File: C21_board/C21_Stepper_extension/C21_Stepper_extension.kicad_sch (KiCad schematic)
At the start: 22 parts, among them J1 Conn_01x04_Male, J10 Conn_01x02_Male, J11 Conn_01x02_Male, J12 Conn_01x04_Male, J2 Conn_01x02_Male, J3 Conn_01x02_Male, J4 Conn_01x02_Male, J5 Jack-DC, J6 Screw_Terminal_01x02, J7 Conn_01x04_Male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

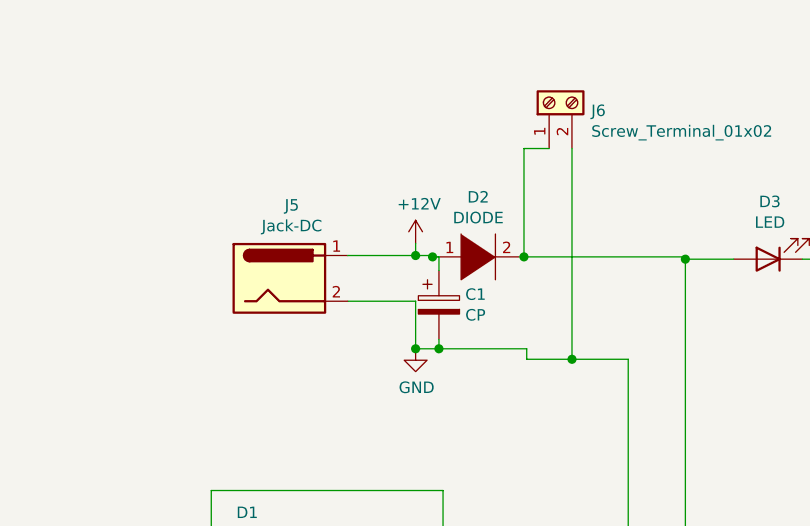
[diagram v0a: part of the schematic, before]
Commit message: add robot arm
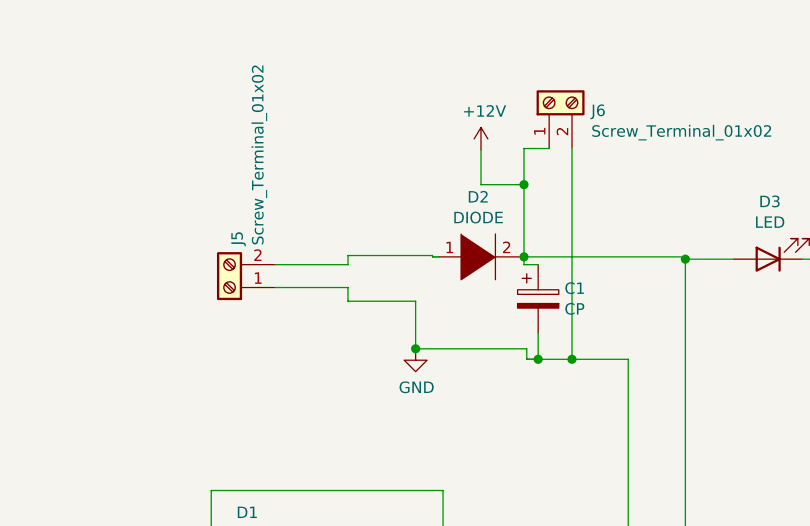
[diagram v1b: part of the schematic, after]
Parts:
- removed J5: Jack-DC, Connector_BarrelJack:BarrelJack_Wuerth_6941xx301002, symbol Connector:Jack-DC
- added J5: Screw_Terminal_01x02, TerminalBlock:TerminalBlock_Altech_AK300-2_P5.00mm, symbol Connector:Screw_Terminal_01x02
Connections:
- net +12V: now also A1.8 (VMOT), A2.8 (VMOT), C2.1, C3.1, D2.2 (A), D3.2 (A), J6.1 (Pin_1); no longer D2.1 (K)
- net GND: now also J5.1 (Pin_1)
- new net: D2.1 (K), J5.2 (Pin_2)
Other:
- moved on the sheet: C1
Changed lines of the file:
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@@
   (junction (at 73.8124 108.0008) (diameter 1.016) (color 0 0 0 0))
   (junction (at 73.8124 114.6556) (diameter 1.016) (color 0 0 0 0))
-  (junction (at 87.9856 44.704) (diameter 1.016) (color 0 0 0 0))
   (junction (at 87.9856 55.0672) (diameter 1.016) (color 0 0 0 0))
-  (junction (at 89.8652 44.8564) (diameter 1.016) (color 0 0 0 0))
-  (junction (at 90.5764 55.0672) (diameter 1.016) (color 0 0 0 0))
   (junction (at 91.0336 88.1888) (diameter 1.016) (color 0 0 0 0))
   (junction (at 91.0336 90.7288) (diameter 1.016) (color 0 0 0 0))
+  (junction (at 100.0252 36.83) (diameter 1.016) (color 0 0 0 0))
   (junction (at 100.0252 44.8564) (diameter 1.016) (color 0 0 0 0))
   (junction (at 101.1936 118.6688) (diameter 1.016) (color 0 0 0 0))
+  (junction (at 101.6 56.2356) (diameter 1.016) (color 0 0 0 0))
   (junction (at 103.7336 118.6688) (diameter 1.016) (color 0 0 0 0))
   (junction (at 105.3592 56.2356) (diameter 1.016) (color 0 0 0 0))
@@
     (stroke (width 0) (type solid) (color 0 0 0 0))
   )
+  (wire (pts (xy 72.39 45.72) (xy 80.4672 45.72))
+    (stroke (width 0) (type solid) (color 0 0 0 0))
+  )
   (wire (pts (xy 72.898 79.6544) (xy 76.6572 79.6544))
     (stroke (width 0) (type solid) (color 0 0 0 0))
@@
     (stroke (width 0) (type solid) (color 0 0 0 0))
   )
-  (wire (pts (xy 80.4672 44.704) (xy 87.9856 44.704))
+  (wire (pts (xy 80.4672 44.704) (xy 89.8652 44.704))
+    (stroke (width 0) (type solid) (color 0 0 0 0))
+  )
+  (wire (pts (xy 80.4672 45.72) (xy 80.4672 44.704))
+    (stroke (width 0) (type solid) (color 0 0 0 0))
+  )
+  (wire (pts (xy 80.4672 48.26) (xy 72.39 48.26))
+    (stroke (width 0) (type solid) (color 0 0 0 0))
+  )
+  (wire (pts (xy 80.4672 49.784) (xy 80.4672 48.26))
     (stroke (width 0) (type solid) (color 0 0 0 0))
   )
@@
     (stroke (width 0) (type solid) (color 0 0 0 0))
   )
-  (wire (pts (xy 87.9856 44.704) (xy 87.9856 43.3324))
-    (stroke (width 0) (type solid) (color 0 0 0 0))
-  )
-  (wire (pts (xy 87.9856 44.704) (xy 89.8652 44.704))
-    (stroke (width 0) (type solid) (color 0 0 0 0))
-  )
   (wire (pts (xy 87.9856 49.784) (xy 87.9856 55.0672))
     (stroke (width 0) (type solid) (color 0 0 0 0))
   )
+  (wire (pts (xy 87.9856 55.0672) (xy 100.33 55.0672))
+    (stroke (width 0) (type solid) (color 0 0 0 0))
+  )
   (wire (pts (xy 89.8652 44.704) (xy 89.8652 44.8564))
     (stroke (width 0) (type solid) (color 0 0 0 0))
@@
     (stroke (width 0) (type solid) (color 0 0 0 0))
   )
-  (wire (pts (xy 90.5764 46.3804) (xy 90.5764 44.8564))
-    (stroke (width 0) (type solid) (color 0 0 0 0))
-  )
-  (wire (pts (xy 90.5764 54.0004) (xy 90.5764 55.0672))
-    (stroke (width 0) (type solid) (color 0 0 0 0))
-  )
-  (wire (pts (xy 90.5764 55.0672) (xy 87.9856 55.0672))
-    (stroke (width 0) (type solid) (color 0 0 0 0))
-  )
   (wire (pts (xy 91.0336 70.8152) (xy 65.278 70.8152))
     (stroke (width 0) (type solid) (color 0 0 0 0))
@@
     (stroke (width 0) (type solid) (color 0 0 0 0))
   )
+  (wire (pts (xy 95.25 33.02) (xy 95.25 36.83))
+    (stroke (width 0) (type solid) (color 0 0 0 0))
+  )
+  (wire (pts (xy 95.25 36.83) (xy 100.0252 36.83))
+    (stroke (width 0) (type solid) (color 0 0 0 0))
+  )
   (wire (pts (xy 100.0252 32.8168) (xy 102.8192 32.8168))
     (stroke (width 0) (type solid) (color 0 0 0 0))
   )
-  (wire (pts (xy 100.0252 44.8564) (xy 100.0252 32.8168))
+  (wire (pts (xy 100.0252 36.83) (xy 100.0252 32.8168))
+    (stroke (width 0) (type solid) (color 0 0 0 0))
+  )
+  (wire (pts (xy 100.0252 44.8564) (xy 100.0252 36.83))
     (stroke (width 0) (type solid) (color 0 0 0 0))
   )
@@
     (stroke (width 0) (type solid) (color 0 0 0 0))
   )
-  (wire (pts (xy 100.33 55.0672) (xy 90.5764 55.0672))
+  (wire (pts (xy 100.0252 45.72) (xy 100.0252 44.8564))
     (stroke (width 0) (type solid) (color 0 0 0 0))
   )
@@
     (stroke (width 0) (type solid) (color 0 0 0 0))
   )
+  (wire (pts (xy 101.6 45.72) (xy 100.0252 45.72))
+    (stroke (width 0) (type solid) (color 0 0 0 0))
+  )
+  (wire (pts (xy 101.6 53.34) (xy 101.6 56.2356))
+    (stroke (width 0) (type solid) (color 0 0 0 0))
+  )
+  (wire (pts (xy 101.6 56.2356) (xy 100.33 56.2356))
+    (stroke (width 0) (type solid) (color 0 0 0 0))
+  )
+  (wire (pts (xy 101.6 56.2356) (xy 100.33 56.2356))
+    (stroke (width 0) (type solid) (color 0 0 0 0))
+  )
   (wire (pts (xy 103.7336 118.6688) (xy 138.4808 118.6688))
     (stroke (width 0) (type solid) (color 0 0 0 0))
@@
     (stroke (width 0) (type solid) (color 0 0 0 0))
   )
-  (wire (pts (xy 105.3592 56.2356) (xy 100.33 56.2356))
+  (wire (pts (xy 105.3592 56.2356) (xy 101.6 56.2356))
     (stroke (width 0) (type solid) (color 0 0 0 0))
   )
@@
     )
   )
-  (symbol (lib_id "power:+12V") (at 87.9856 43.3324 0) (unit 1)
-    (in_bom yes) (on_board yes)
-    (property "Reference" "#PWR0108" (id 0) (at 87.9856 47.1424 0)
-      (effects (font (size 1.27 1.27)) hide)
-    )
-    (property "Value" "+12V" (id 1) (at 88.3539 39.008 0))
-    (property "Footprint" "" (id 2) (at 87.9856 43.3324 0)
-      (effects (font (size 1.27 1.27)) hide)
-    )
-    (property "Datasheet" "" (id 3) (at 87.9856 43.3324 0)
+  (symbol (lib_id "power:+12V") (at 95.25 33.02 0) (unit 1)
+    (in_bom yes) (on_board yes)
+    (property "Reference" "#PWR0108" (id 0) (at 95.25 36.83 0)
+      (effects (font (size 1.27 1.27)) hide)
+    )
+    (property "Value" "+12V" (id 1) (at 95.6183 28.6956 0))
+    (property "Footprint" "" (id 2) (at 95.25 33.02 0)
+      (effects (font (size 1.27 1.27)) hide)
+    )
+    (property "Datasheet" "" (id 3) (at 95.25 33.02 0)
       (effects (font (size 1.27 1.27)) hide)
     )
@@
     )
   )
+  (symbol (lib_id "Connector:Screw_Terminal_01x02") (at 67.31 48.26 180) (unit 1)
+    (in_bom yes) (on_board yes)
+    (property "Reference" "J5" (id 0) (at 68.1926 43.5863 90)
+      (effects (font (size 1.27 1.27)) (justify right))
+    )
+    (property "Value" "Screw_Terminal_01x02" (id 1) (at 70.4913 43.5863 90)
+      (effects (font (size 1.27 1.27)) (justify right))
+    )
+    (property "Footprint" "TerminalBlock:TerminalBlock_Altech_AK300-2_P5.00mm" (id 2) (at 67.31 48.26 0)
+      (effects (font (size 1.27 1.27)) hide)
+    )
+    (property "Datasheet" "~" (id 3) (at 67.31 48.26 0)
+      (effects (font (size 1.27 1.27)) hide)
+    )
+  )
   (symbol (lib_id "Connector:Screw_Terminal_01x02") (at 102.8192 27.7368 90) (unit 1)
     (in_bom yes) (on_board yes)
@@
     )
   )
-  (symbol (lib_id "Device:CP") (at 90.5764 50.1904 0) (unit 1)
-    (in_bom yes) (on_board yes)
-    (property "Reference" "C1" (id 0) (at 93.4975 49.041 0)
+  (symbol (lib_id "Device:CP") (at 101.6 49.53 0) (unit 1)
+    (in_bom yes) (on_board yes)
+    (property "Reference" "C1" (id 0) (at 104.5211 48.3806 0)
       (effects (font (size 1.27 1.27)) (justify left))
     )
-    (property "Value" "CP" (id 1) (at 93.4975 51.3397 0)
+    (property "Value" "CP" (id 1) (at 104.5211 50.6793 0)
       (effects (font (size 1.27 1.27)) (justify left))
     )
-    (property "Footprint" "Capacitor_THT:CP_Radial_D8.0mm_P2.50mm" (id 2) (at 91.5416 54.0004 0)
-      (effects (font (size 1.27 1.27)) hide)
-    )
-    (property "Datasheet" "~" (id 3) (at 90.5764 50.1904 0)
+    (property "Footprint" "Capacitor_THT:CP_Radial_D8.0mm_P2.50mm" (id 2) (at 102.5652 53.34 0)
+      (effects (font (size 1.27 1.27)) hide)
+    )
+    (property "Datasheet" "~" (id 3) (at 101.6 49.53 0)
       (effects (font (size 1.27 1.27)) hide)
     )
@@
     )
     (property "Datasheet" "~" (id 3) (at 94.9452 44.8564 0)
-      (effects (font (size 1.27 1.27)) hide)
-    )
-  )
-  (symbol (lib_id "Connector:Jack-DC") (at 72.8472 47.244 0) (unit 1)
-    (in_bom yes) (on_board yes)
-    (property "Reference" "J5" (id 0) (at 74.2442 39.1222 0))
-    (property "Value" "Jack-DC" (id 1) (at 74.2442 41.4209 0))
-    (property "Footprint" "Connector_BarrelJack:BarrelJack_Wuerth_6941xx301002" (id 2) (at 74.1172 48.26 0)
-      (effects (font (size 1.27 1.27)) hide)
-    )
-    (property "Datasheet" "~" (id 3) (at 74.1172 48.26 0)
       (effects (font (size 1.27 1.27)) hide)
     )
@@
       (reference "J4") (unit 1) (value "Conn_01x02_Male") (footprint "Connector_PinSocket_2.54mm:PinSocket_1x02_P2.54mm_Vertical")
     )
-    (path "/c8d7e6f1-8ef5-4150-af9e-0d65907873f1"
-      (reference "J5") (unit 1) (value "Jack-DC") (footprint "Connector_BarrelJack:BarrelJack_Wuerth_6941xx301002")
+    (path "/9ba4e808-dcc0-46c7-af7c-de85dc4615e8"
+      (reference "J5") (unit 1) (value "Screw_Terminal_01x02") (footprint "TerminalBlock:TerminalBlock_Altech_AK300-2_P5.00mm")
     )
     (path "/23f4a1d0-9678-4fde-9629-279acb1e9eb5"
